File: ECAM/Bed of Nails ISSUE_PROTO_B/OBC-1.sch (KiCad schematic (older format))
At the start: 26 parts

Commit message: saving out files
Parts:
- gave numbers to parts that had none: 7
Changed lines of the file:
@@
 	4000 1600 4000 1400
 $Comp
-L TFT_testpoints:TEST-POINT TP?
+L TFT_testpoints:TEST-POINT TP16
 U 1 1 60CC4740
 P 4900 1500
-F 0 "TP?" H 4700 1500 50  0000 C CNN
+F 0 "TP16" H 4700 1500 50  0000 C CNN
 F 1 "TEST-POINT" H 4900 1850 50  0001 C CNN
 F 2 "TFT_TestPoints:TP_RDPad_D1.0mm" H 4900 1500 50  0001 C CNN
@@
 	3750 2850 3950 2850
 $Comp
-L TFT_testpoints:TEST-POINT TP?
+L TFT_testpoints:TEST-POINT TP19
 U 1 1 60CCBFF5
 P 4900 1700
-F 0 "TP?" H 4700 1700 50  0000 C CNN
+F 0 "TP19" H 4700 1700 50  0000 C CNN
 F 1 "TEST-POINT" H 4900 2050 50  0001 C CNN
 F 2 "TFT_TestPoints:TP_RDPad_D1.0mm" H 4900 1700 50  0001 C CNN
@@
 $EndComp
 $Comp
-L TFT_testpoints:TEST-POINT TP?
+L TFT_testpoints:TEST-POINT TP30
 U 1 1 60CCC4BB
 P 4900 1800
-F 0 "TP?" H 4700 1800 50  0000 C CNN
+F 0 "TP30" H 4700 1800 50  0000 C CNN
 F 1 "TEST-POINT" H 4900 2150 50  0001 C CNN
 F 2 "TFT_TestPoints:TP_RDPad_D1.0mm" H 4900 1800 50  0001 C CNN
@@
 $EndComp
 $Comp
-L TFT_testpoints:TEST-POINT TP?
+L TFT_testpoints:TEST-POINT TP31
 U 1 1 60CCF1A5
 P 4900 2000
-F 0 "TP?" H 4700 2000 50  0000 C CNN
+F 0 "TP31" H 4700 2000 50  0000 C CNN
 F 1 "TEST-POINT" H 4900 2350 50  0001 C CNN
 F 2 "TFT_TestPoints:TP_RDPad_D1.0mm" H 4900 2000 50  0001 C CNN
@@
 $EndComp
 $Comp
-L TFT_testpoints:TEST-POINT TP?
+L TFT_testpoints:TEST-POINT TP32
 U 1 1 60CCF1AB
 P 4900 2100
-F 0 "TP?" H 4700 2100 50  0000 C CNN
+F 0 "TP32" H 4700 2100 50  0000 C CNN
 F 1 "TEST-POINT" H 4900 2450 50  0001 C CNN
 F 2 "TFT_TestPoints:TP_RDPad_D1.0mm" H 4900 2100 50  0001 C CNN
@@
 $EndComp
 $Comp
-L TFT_testpoints:TEST-POINT TP?
+L TFT_testpoints:TEST-POINT TP33
 U 1 1 60CD0063
 P 4900 2300
-F 0 "TP?" H 4700 2300 50  0000 C CNN
+F 0 "TP33" H 4700 2300 50  0000 C CNN
 F 1 "TEST-POINT" H 4900 2650 50  0001 C CNN
 F 2 "TFT_TestPoints:TP_RDPad_D1.0mm" H 4900 2300 50  0001 C CNN
@@
 $EndComp
 $Comp
-L TFT_testpoints:TEST-POINT TP?
+L TFT_testpoints:TEST-POINT TP34
 U 1 1 60CD0069
 P 4900 2400
-F 0 "TP?" H 4700 2400 50  0000 C CNN
+F 0 "TP34" H 4700 2400 50  0000 C CNN
 F 1 "TEST-POINT" H 4900 2750 50  0001 C CNN
 F 2 "TFT_TestPoints:TP_RDPad_D1.0mm" H 4900 2400 50  0001 C CNN

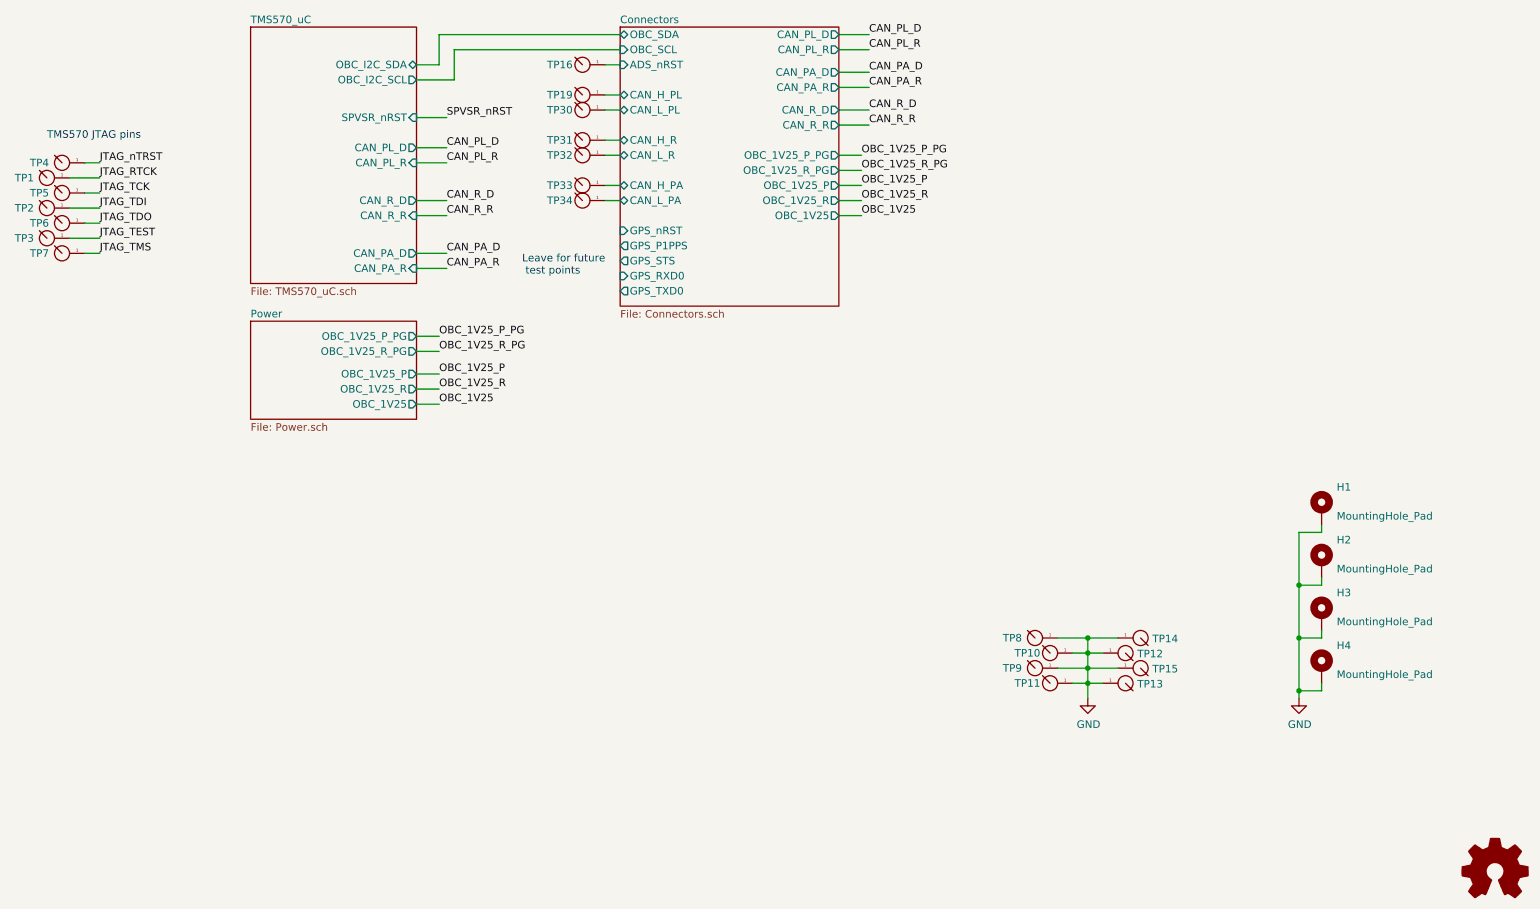
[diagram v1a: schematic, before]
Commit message: updated title blocks and testpoint/connector passthroughs
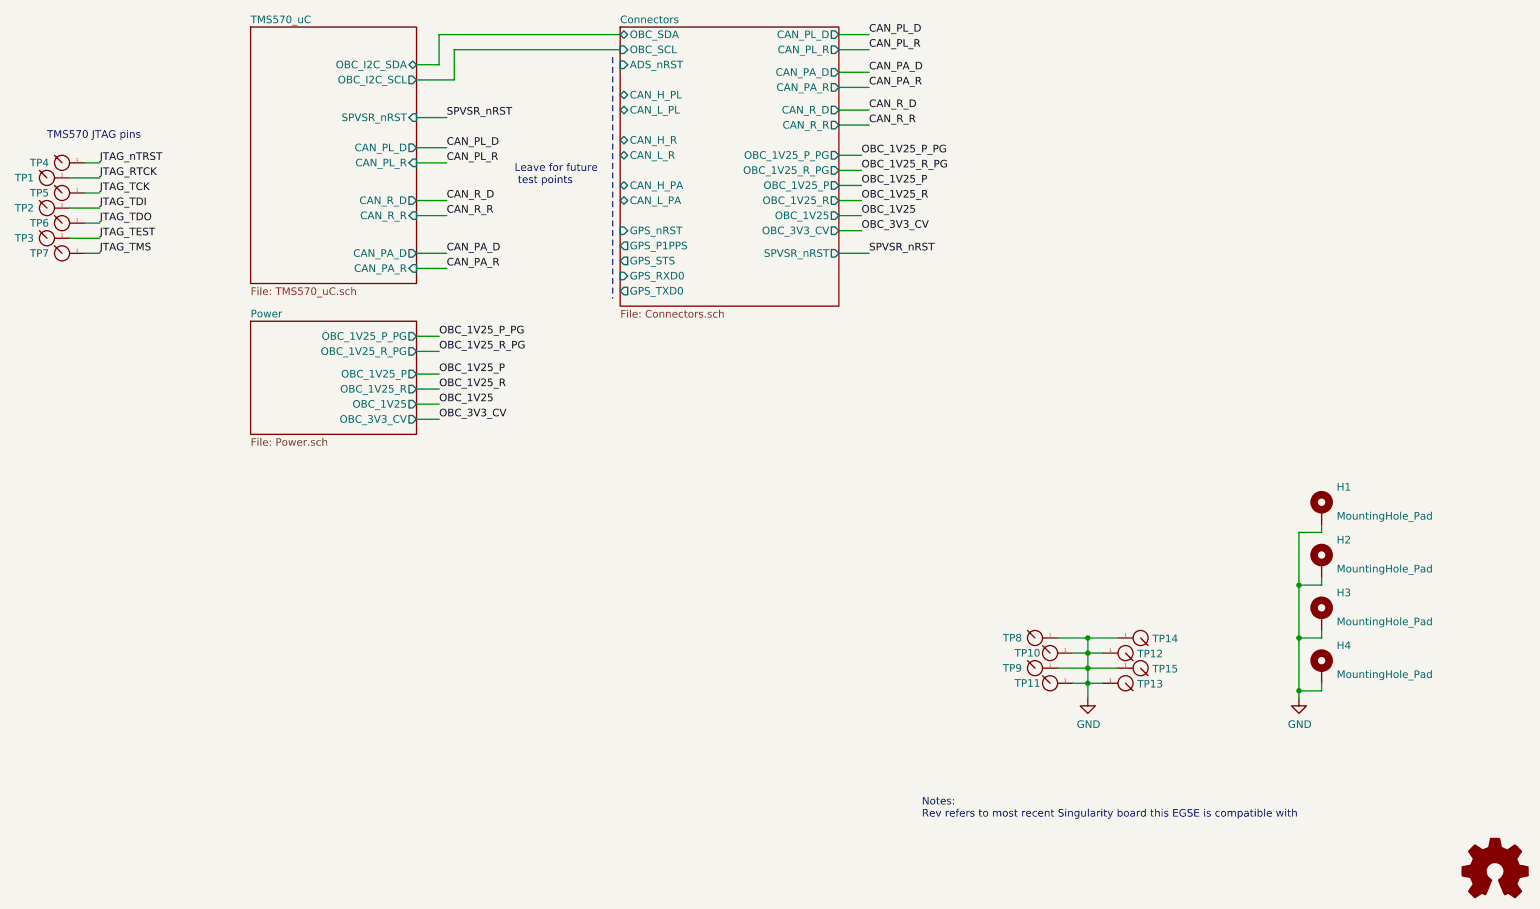
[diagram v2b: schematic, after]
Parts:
- removed TP16, TP19, TP30, TP31, TP32, TP33, TP34: TEST-POINT, TFT_TestPoints:TP_RDPad_D1.0mm, symbol TFT_testpoints:TEST-POINT
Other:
- note added: "Notes:\nRev refers to most recent Singularity board this EGSE is compatible with"
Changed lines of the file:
@@
 encoding utf-8
 Sheet 1 4
-Title "Singularity OBC - Top Level Architecture"
-Date "2021-05-24"
-Rev "PROTO_B_v01"
+Title "Singularity EGSE - Top Level Architecture"
+Date "2021-06-05"
+Rev "PROTO_B_v02"
 Comp "The Flame Trench"
 Comment1 "Drawn by:  Ben Cartwright"
@@
 F25 "OBC_1V25_R" O R 6550 2400 50
 F26 "OBC_1V25" O R 6550 2500 50
+F27 "OBC_3V3_CV" O R 6550 2600 50
+F28 "SPVSR_nRST" O R 6550 2750 50
 $EndSheet
 $Comp
@@
 	1550 2150 1650 2150
 $Sheet
-S 2650 3200 1100 650
+S 2650 3200 1100 750
 U 607BD428
 F0 "Power" 50
@@
 F5 "OBC_1V25_R" O R 3750 3650 50
 F6 "OBC_1V25" O R 3750 3750 50
+F7 "OBC_3V3_CV" O R 3750 3850 50
 $EndSheet
 $Comp
@@
 Wire Wire Line
 	4000 1600 4000 1400
-$Comp
-L TFT_testpoints:TEST-POINT TP16
-U 1 1 60CC4740
-P 4900 1500
-F 0 "TP16" H 4700 1500 50  0000 C CNN
-F 1 "TEST-POINT" H 4900 1850 50  0001 C CNN
-F 2 "TFT_TestPoints:TP_RDPad_D1.0mm" H 4900 1500 50  0001 C CNN
-F 3 "" H 4900 1500 50  0001 C CNN
-	1    4900 1500
-	1    0    0    -1
-$EndComp
 Text Label 3950 1850 0    50   ~ 0
 SPVSR_nRST
@@
 Wire Wire Line
 	3750 2850 3950 2850
-$Comp
-L TFT_testpoints:TEST-POINT TP19
-U 1 1 60CCBFF5
-P 4900 1700
-F 0 "TP19" H 4700 1700 50  0000 C CNN
-F 1 "TEST-POINT" H 4900 2050 50  0001 C CNN
-F 2 "TFT_TestPoints:TP_RDPad_D1.0mm" H 4900 1700 50  0001 C CNN
-F 3 "" H 4900 1700 50  0001 C CNN
-	1    4900 1700
-	1    0    0    -1
-$EndComp
-$Comp
-L TFT_testpoints:TEST-POINT TP30
-U 1 1 60CCC4BB
-P 4900 1800
-F 0 "TP30" H 4700 1800 50  0000 C CNN
-F 1 "TEST-POINT" H 4900 2150 50  0001 C CNN
-F 2 "TFT_TestPoints:TP_RDPad_D1.0mm" H 4900 1800 50  0001 C CNN
-F 3 "" H 4900 1800 50  0001 C CNN
-	1    4900 1800
-	1    0    0    -1
-$EndComp
-$Comp
-L TFT_testpoints:TEST-POINT TP31
-U 1 1 60CCF1A5
-P 4900 2000
-F 0 "TP31" H 4700 2000 50  0000 C CNN
-F 1 "TEST-POINT" H 4900 2350 50  0001 C CNN
-F 2 "TFT_TestPoints:TP_RDPad_D1.0mm" H 4900 2000 50  0001 C CNN
-F 3 "" H 4900 2000 50  0001 C CNN
-	1    4900 2000
-	1    0    0    -1
-$EndComp
-$Comp
-L TFT_testpoints:TEST-POINT TP32
-U 1 1 60CCF1AB
-P 4900 2100
-F 0 "TP32" H 4700 2100 50  0000 C CNN
-F 1 "TEST-POINT" H 4900 2450 50  0001 C CNN
-F 2 "TFT_TestPoints:TP_RDPad_D1.0mm" H 4900 2100 50  0001 C CNN
-F 3 "" H 4900 2100 50  0001 C CNN
-	1    4900 2100
-	1    0    0    -1
-$EndComp
-$Comp
-L TFT_testpoints:TEST-POINT TP33
-U 1 1 60CD0063
-P 4900 2300
-F 0 "TP33" H 4700 2300 50  0000 C CNN
-F 1 "TEST-POINT" H 4900 2650 50  0001 C CNN
-F 2 "TFT_TestPoints:TP_RDPad_D1.0mm" H 4900 2300 50  0001 C CNN
-F 3 "" H 4900 2300 50  0001 C CNN
-	1    4900 2300
-	1    0    0    -1
-$EndComp
-$Comp
-L TFT_testpoints:TEST-POINT TP34
-U 1 1 60CD0069
-P 4900 2400
-F 0 "TP34" H 4700 2400 50  0000 C CNN
-F 1 "TEST-POINT" H 4900 2750 50  0001 C CNN
-F 2 "TFT_TestPoints:TP_RDPad_D1.0mm" H 4900 2400 50  0001 C CNN
-F 3 "" H 4900 2400 50  0001 C CNN
-	1    4900 2400
-	1    0    0    -1
-$EndComp
-Wire Wire Line
-	5000 1700 5100 1700
-Wire Wire Line
-	5100 1800 5000 1800
-Wire Wire Line
-	5000 2000 5100 2000
-Wire Wire Line
-	5000 2100 5100 2100
-Wire Wire Line
-	5000 2300 5100 2300
-Wire Wire Line
-	5000 2400 5100 2400
-Text Notes 4450 2900 0    50   ~ 0
+Text Notes 4400 2300 0    50   ~ 0
 Leave for future\n test points
 Wire Wire Line
@@
 OBC_1V25
 Wire Wire Line
-	5000 1500 5100 1500
-Wire Wire Line
 	6550 2100 6700 2100
 Wire Wire Line
@@
 Text Label 6700 2500 0    50   ~ 0
 OBC_1V25
+Wire Wire Line
+	3750 3850 3900 3850
+Text Label 3900 3850 0    50   ~ 0
+OBC_3V3_CV
+Wire Wire Line
+	6550 2600 6700 2600
+Text Label 6700 2600 0    50   ~ 0
+OBC_3V3_CV
+Wire Notes Line
+	5050 1450 5050 3050
+Text Label 6750 2750 0    50   ~ 0
+SPVSR_nRST
+Wire Wire Line
+	6750 2750 6550 2750
+Text Notes 7100 6500 0    50   ~ 0
+Notes:\nRev refers to most recent Singularity board this EGSE is compatible with
 $EndSCHEMATC

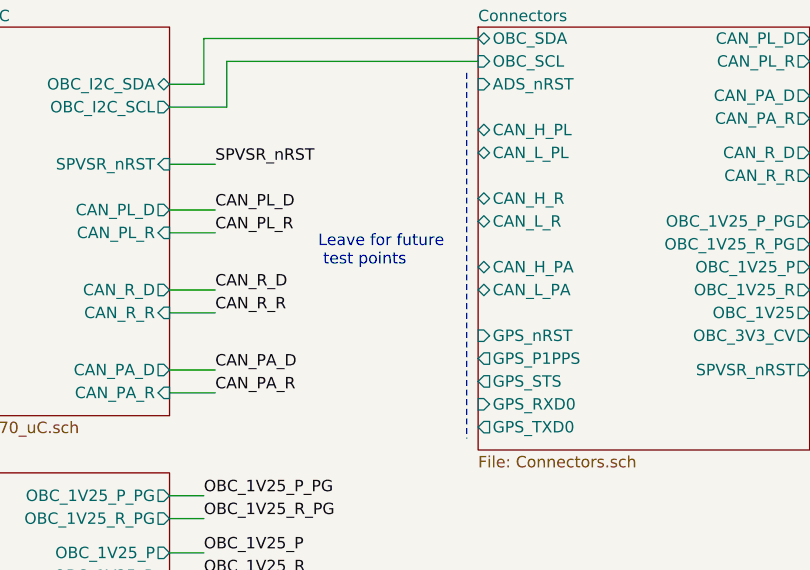
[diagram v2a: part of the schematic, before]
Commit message: updated text labelling
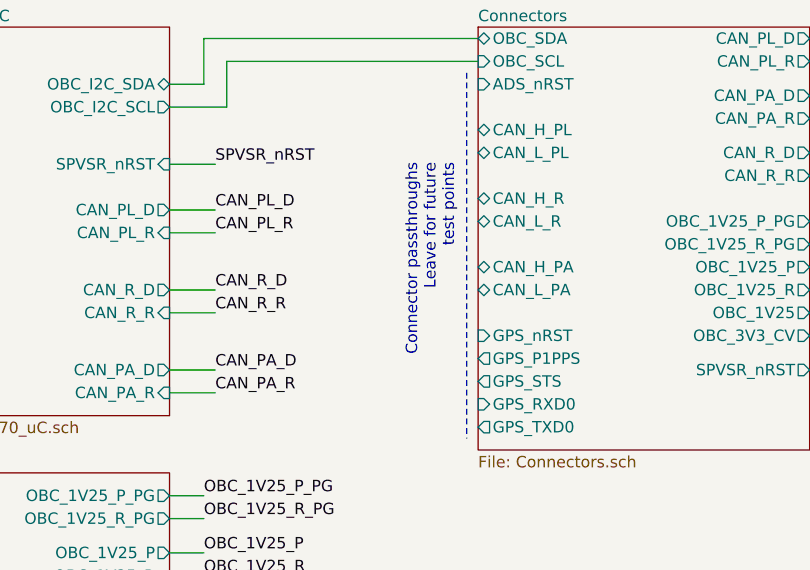
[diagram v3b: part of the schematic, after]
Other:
- note added: "Connector passthroughs\nLeave for future\ntest points"
- note removed: "Leave for future\n test points"
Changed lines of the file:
@@
 Wire Wire Line
 	3750 2850 3950 2850
-Text Notes 4400 2300 0    50   ~ 0
-Leave for future\n test points
+Text Notes 5000 1850 3    50   ~ 0
+Connector passthroughs\nLeave for future\ntest points
 Wire Wire Line
 	3900 1300 5100 1300
